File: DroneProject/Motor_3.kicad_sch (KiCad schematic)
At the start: 0 parts

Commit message: Finished motor and C1 designs, still need to rename components on MTR2, 3, and 4 pages
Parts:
- added C17, C20: 1uF, Capacitor_SMD:C_0402_1005Metric, symbol Device:C
- added C18: 10uF, Capacitor_SMD:C_1206_3216Metric, symbol Device:C
- added C19, C28, C39: 0.1uF, Capacitor_SMD:C_0402_1005Metric, symbol Device:C
- added C21: 47nF, Capacitor_SMD:C_0402_1005Metric, symbol Device:C
- added C22, C23: 270uF, Capacitor_SMD:CP_Elec_10x10.5, symbol Device:C_Polarized
- added C24, C25, C26, C27, C29, C30: 1uF, Capacitor_SMD:C_0603_1608Metric, symbol Device:C
- added NT5, NT6, NT7, NT8: NetTie_2, NetTie:NetTie-2_SMD_Pad0.5mm, symbol Device:NetTie_2
- added Q10, Q11, Q12, Q7, Q8, Q9: CSD17577Q5A, Package_TO_SOT_SMD:TDSON-8-1, symbol Transistor_FET:CSD17577Q5A
- added R10: 33, Resistor_SMD:R_0402_1005Metric, symbol Device:R_US
- added R11, R12: CSS2H-2512K-2L00J, Resistor_SMD:R_2512_6332Metric, symbol Device:R
- added R7, R8, R9: 10K, Resistor_SMD:R_0402_1005Metric, symbol Device:R_US
- added U4: DRV8320SRTVR, Library:DRV8320SRTVR, symbol Global:DRV8320SRTVR
- added U5, U6: INA180A2, Package_TO_SOT_SMD:SOT-23-5, symbol Amplifier_Current:INA180A2
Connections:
- new net: NT5.2, U5.3 (+)
- new net: NT6.2, U5.4 (-)
- new net: Q9.4 (G), U4.12 (GHB)
- new net: NT8.2, U6.4 (-)
- new net: C21.1, U4.32 (CPL)
- new net: C21.2, U4.1 (CPH)
- new net: C20.2, U4.2 (VCP)
- new net: NT7.1, Q10.1 (S), Q10.2 (S), Q10.3 (S), R12.1, U4.9 (SLB)
- new net: NT7.2, U6.3 (+)
- new net: R10.2, U4.18 (SDO)
- new net: Q10.4 (G), U4.10 (GLB)
- new net: NT5.1, Q8.1 (S), Q8.2 (S), Q8.3 (S), R11.1, U4.8 (SLA)
- new net: Q8.4 (G), U4.7 (GLA)
- new net: Q7.4 (G), U4.5 (GHA)
- new net: Q11.4 (G), U4.13 (GHC)
- new net: Q12.4 (G), U4.15 (GLC)
- new net +3.3V: C28.1, C39.1, R7.2, R8.2, R9.2, U5.5 (V+), U6.5 (V+)
- new net C1_SPI2_MISO: R10.1
- new net C1_SPI2_MOSI: U4.19 (SDI)
- new net C1_SPI2_SCK: U4.20 (SCK)
- new net GND: C17.2, C28.2, C39.2, U4.23 (AGND), U4.33 (PAD), U5.2 (GND), U6.2 (GND)
- new net GNDPWR: C18.2, C19.2, C22.2, C23.2, C24.2, C25.2, C26.2, C27.2, C29.2, C30.2, NT6.1, NT8.1, Q12.1 (S), Q12.2 (S), Q12.3 (S), R11.2, R12.2, U4.16 (SLC), U4.31 (PGND)
- new net MTR1_DVDD: C17.1, U4.24 (DVDD)
- new net MTR3_A: Q7.1 (S), Q7.2 (S), Q7.3 (S), Q8.5 (D), U4.6 (SHA)
- new net MTR3_A_PWM: U4.25 (INHA)
- new net MTR3_B: Q10.5 (D), Q9.1 (S), Q9.2 (S), Q9.3 (S), U4.11 (SHB)
- new net MTR3_B_PWM: U4.27 (INHB)
- new net MTR3_C: Q11.1 (S), Q11.2 (S), Q11.3 (S), Q12.5 (D), U4.14 (SHC)
- new net MTR3_CSN: R9.1, U4.21 (nSCS)
- new net MTR3_CURR_A: U5.1
- new net MTR3_CURR_B: U6.1
- new net MTR3_C_PWM: U4.29 (INHC)
- new net MTR3_EN: R8.1, U4.22 (ENABLE)
- new net MTR3_FAULT_N: R7.1, U4.17 (FAULT_N)
- new net VDD: C18.1, C19.1, C20.1, C22.1, C23.1, C24.1, C25.1, C26.1, C27.1, C29.1, C30.1, Q11.5 (D), Q7.5 (D), Q9.5 (D), U4.3 (VM), U4.4 (VDRAIN)

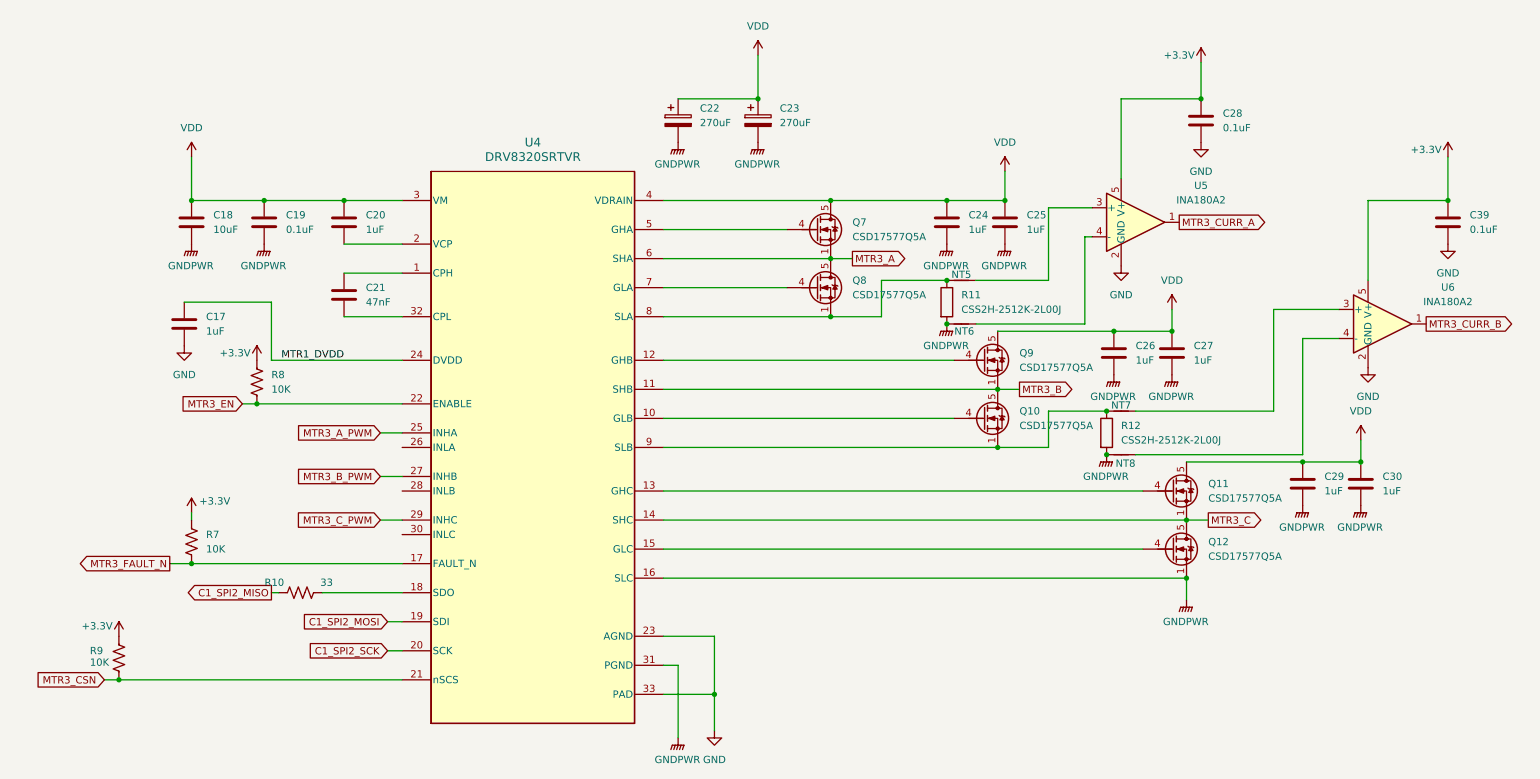
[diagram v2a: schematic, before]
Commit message: Finished most of routing for motor controls, however likely going to revert back and make separate ESC boards for motor control as I think that would honestly be more efficient from both a cost and debug complexity standpoint.
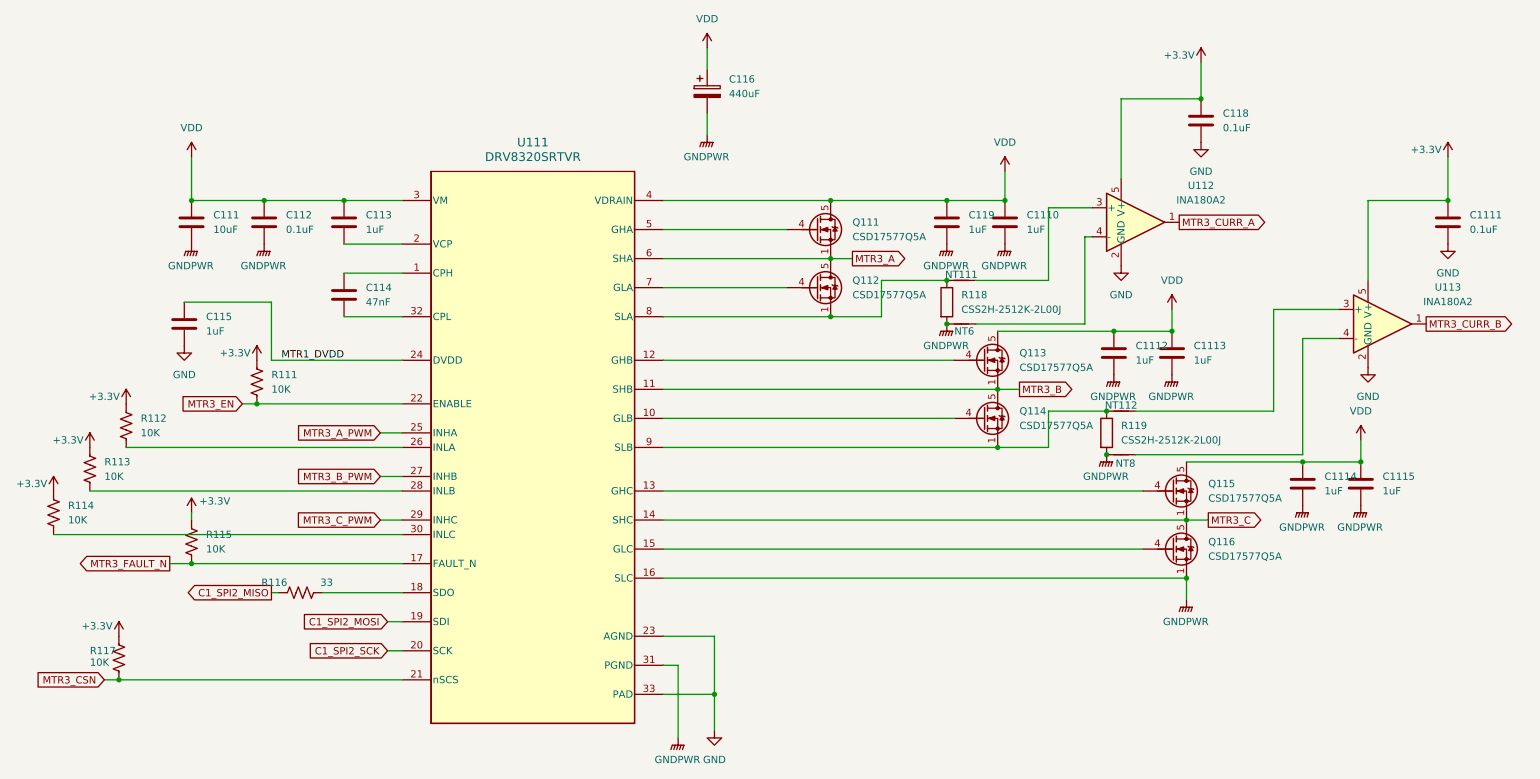
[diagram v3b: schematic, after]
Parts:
- removed C22, C23: 270uF, Capacitor_SMD:CP_Elec_10x10.5, symbol Device:C_Polarized
- added C116: 440uF, Capacitor_THT:CP_Radial_D10.0mm_P5.00mm, symbol Device:C_Polarized
- added R112, R113, R114: 10K, Resistor_SMD:R_0402_1005Metric, symbol Device:R_US
- renumbered C18 to C111, C25 to C1110, C39 to C1111, C26 to C1112, C27 to C1113, C29 to C1114, C30 to C1115, C19 to C112, C20 to C113, C21 to C114, C17 to C115, C28 to C118, C24 to C119, NT5 to NT111, NT7 to NT112, Q7 to Q111, Q8 to Q112, Q9 to Q113, Q10 to Q114, Q11 to Q115, Q12 to Q116, R8 to R111, R7 to R115, R10 to R116, R9 to R117, R11 to R118, R12 to R119, U4 to U111, U5 to U112, U6 to U113
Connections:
- net +3.3V: now also R112.2, R113.2, R114.2
- net GNDPWR: now also C116.2
- net VDD: now also C116.1
- net at U111.26 (INLA): now also R112.1
- net at U111.28 (INLB): now also R113.1
- net at U111.30 (INLC): now also R114.1
